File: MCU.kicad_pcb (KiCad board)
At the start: 2 copper layers, 55.9 x 30.5 mm, 55 parts, among them CON1 BARREL_JACK, P1 CONN_01X14, P2 CONN_01X14, P3 CONN_01X09, P4 USB_OTG, P5 CONN_02X05, P6 CONN_01X09, P7 CONN_02X04, P8 USB_OTG, SW1 Reset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

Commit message: Added Analog-Digital Conversion Capability
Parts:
- added C22: 0.1uF, Capacitors_SMD:C_0603, F.Cu at (-8.00, -23.0)
- added C23: 0.1uF, Capacitors_SMD:C_0603, F.Cu at (-12.4, -23.2)
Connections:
- net /LED-Feedback renamed /LED-FB
- U1 pad 13: Net-(U1-Pad13) -> +3V3
- U1 pad 14: Net-(U1-Pad14) -> +3V3
- U1 pad 15: Net-(U1-Pad15) -> GND
- U1 pad 16: Net-(U1-Pad16) -> GND
- U1 pad 17: Net-(U1-Pad17) -> +3V3
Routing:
- net +3V3: track 73.9 -> 83.6 mm
- net GND: track 41.0 -> 41.8 mm, vias 48 -> 51
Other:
- board text removed: "Flash Header"

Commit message: Made PCB more Manufacturer-friendly
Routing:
- net /D-: track 15.1 -> 19.4 mm
- net /PTB19: track 10.2 -> 7.57 mm
- net /PTB18: track 14.2 -> 11.9 mm
- net /PTB17: track 12.9 -> 10.8 mm
- net /PTB16: track 14.2 -> 13.5 mm
- net /INTB: track 5.74 -> 5.02 mm

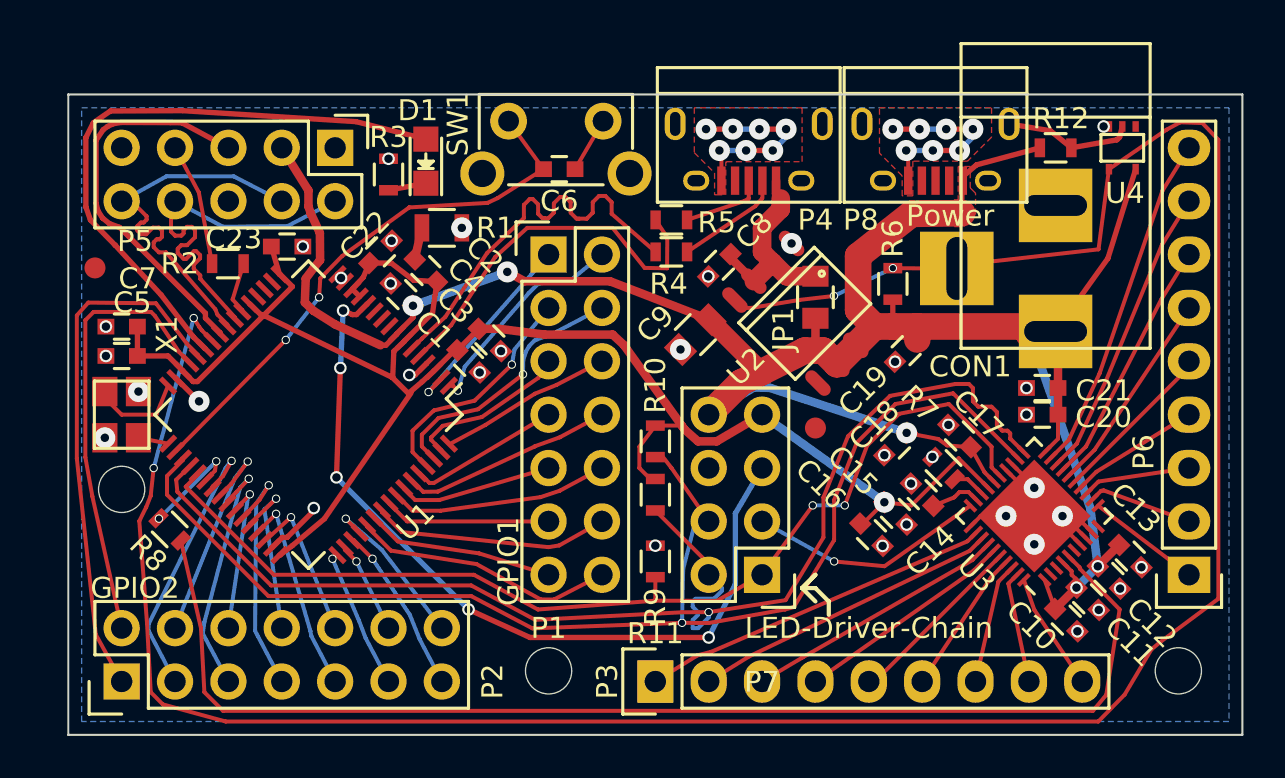
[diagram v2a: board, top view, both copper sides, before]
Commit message: Switched to 2.5mm Mounting Holes
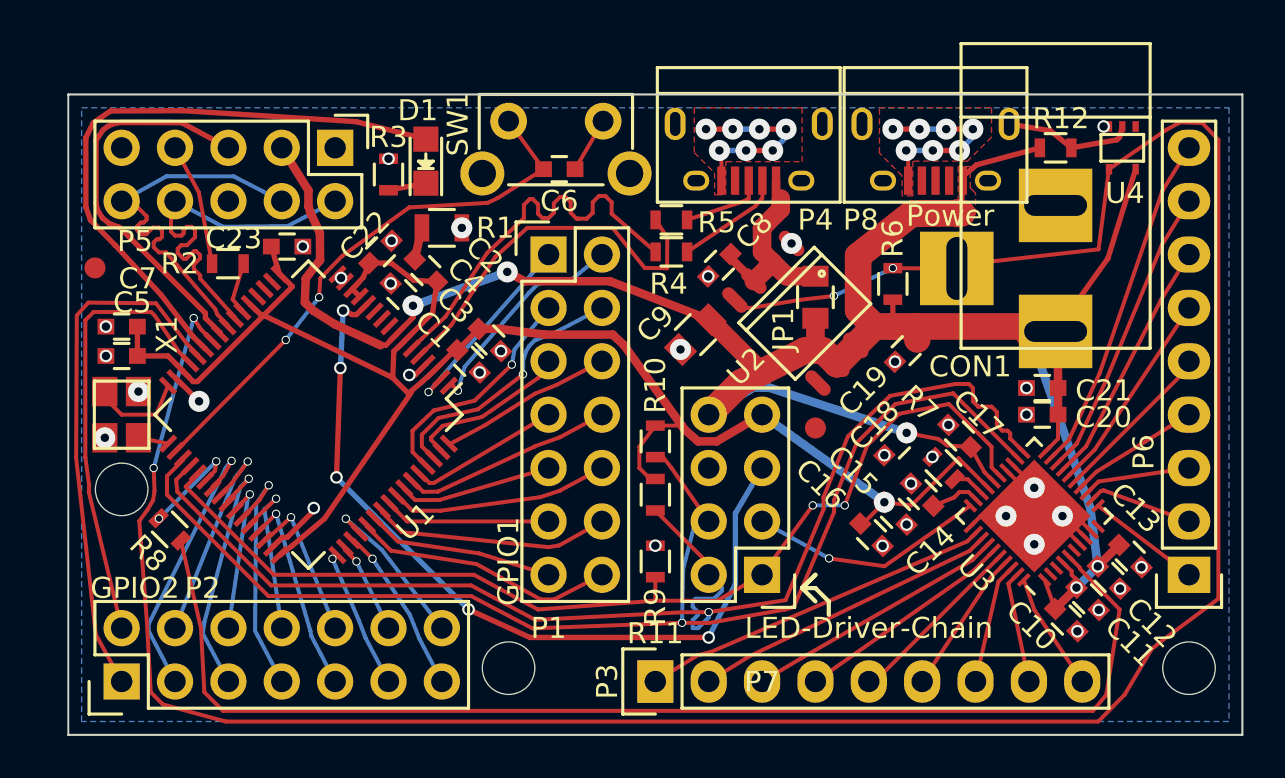
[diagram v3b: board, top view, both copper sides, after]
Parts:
- removed the ? at (-20.3, -11.7)
- removed the ? at (0.00, -3.05)
- removed the ? at (30.0, -3.05)
- added ?: MountingHole_2.5mm, Mounting_Holes:MountingHole_2.5mm, F.Cu at (-20.3, -11.7)
- added ?: MountingHole_2.5mm, Mounting_Holes:MountingHole_2.5mm, F.Cu at (30.5, -3.17)
- added ?: MountingHole_2.5mm, Mounting_Holes:MountingHole_2.5mm, F.Cu at (-1.91, -3.17)

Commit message: More appropriate Placement of Mounting-Holes
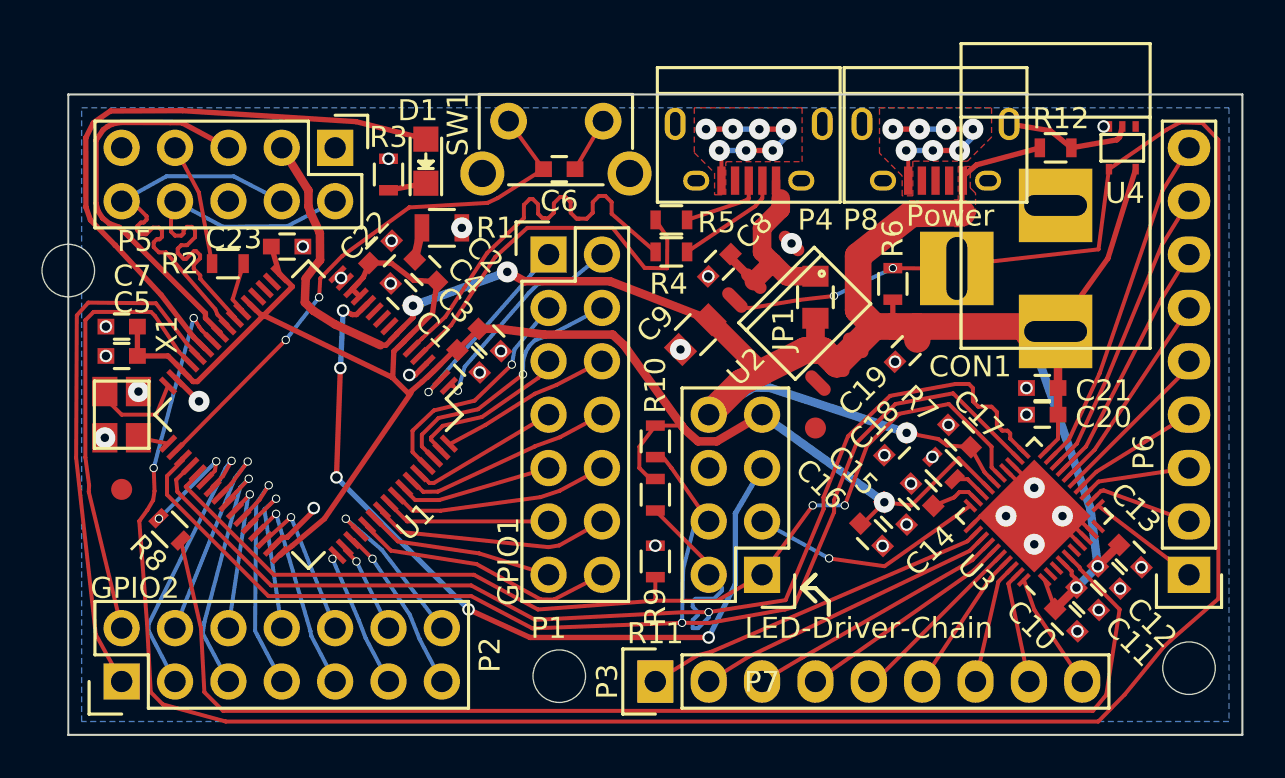
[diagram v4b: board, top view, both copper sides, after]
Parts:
- moved ? 10.7 mm to (-22.9, -22.1)
- moved ? 10.6 mm to (-20.3, -11.7)
- moved ? 2.44 mm to (0.51, -2.79)
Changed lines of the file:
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@@
     (links 185)
     (no_connects 0)
-    (area -38.606296 -33.8682 43.607343 2.571533)
+    (area -22.909551 -30.529551 33.069551 0.049551)
     (thickness 1.6002)
     (drawings 14)
@@
   )
   (module Mounting_Holes:MountingHole_2.5mm (layer Front)
-    (at -20.32 -11.684)
+    (at -22.86 -22.098)
     (descr "Mounting Hole 2.5mm, no annular")
     (tags "mounting hole 2.5mm no annular")
@@
     (descr "Through hole pin header")
     (tags "pin header")
-    (fp_text reference P2 (at 4.445 3.8481 180) (layer F.SilkS)
+    (fp_text reference P2 (at 1.27 17.526 90) (layer F.SilkS)
       (effects (font (size 1 1) (thickness 0.15)))
     )
@@
     (tags "capacitor 0603")
     (attr smd)
-    (fp_text reference C7 (at -0.762 2.286 180) (layer F.SilkS)
+    (fp_text reference C7 (at -0.508 2.413 180) (layer F.SilkS)
       (effects (font (size 1 1) (thickness 0.15)))
     )
@@
   )
   (module Fiducials:Fiducial_1mm_Dia_2.54mm_Outer_CopperTop (layer Front)
-    (at -21.59 -22.225)
+    (at -20.32 -11.684)
     (descr "Circular Fiducial, 1mm bare copper top; 2.54mm keepout")
     (tags marker)
@@
   )
   (module Mounting_Holes:MountingHole_2.5mm (layer Front)
-    (at -1.905 -3.175)
+    (at 0.508 -2.794)
     (descr "Mounting Hole 2.5mm, no annular")
     (tags "mounting hole 2.5mm no annular")
@@
   (segment (start 8.65833 -22.701645) (end 9.767331 -21.592644) (width 0.4064) (layer Front) (net 75) (status 30))
   (segment (start 10.9855 -22.170525) (end 10.665356 -22.490669) (width 0.4064) (layer Front) (net 75) (status 30))
-  (segment (start 27.417892 -1.918801) (end 28.692825 -4.069439) (width 0.19) (layer Front) (net 76))
-  (segment (start 29.107569 -4.41556) (end 31.877 -6.477) (width 0.19) (layer Front) (net 76))
-  (segment (start 28.692825 -4.069439) (end 29.107569 -4.41556) (width 0.19) (layer Front) (net 76))
+  (segment (start 27.417892 -1.918801) (end 29.294566 -4.207434) (width 0.19) (layer Front) (net 76))
+  (segment (start 29.594871 -4.487622) (end 31.877 -6.477) (width 0.19) (layer Front) (net 76))
+  (segment (start 29.294566 -4.207434) (end 29.594871 -4.487622) (width 0.19) (layer Front) (net 76))
   (via (at 13.581769 -20.890666) (size 0.4) (drill 0.3) (layers Front Back) (net 76))
   (segment (start 13.581769 -20.890666) (end 11.938 -20.701) (width 0.19) (layer Front) (net 76))
@@
   (segment (start -18.923 -20.1295) (end -21.6535 -20.1295) (width 0.19) (layer Front) (net 83))
   (segment (start -21.6535 -20.1295) (end -22.0472 -19.7358) (width 0.19) (layer Front) (net 83))
-  (segment (start -20.32 -5.08) (end -20.32 -5.08) (width 0.19) (layer Front) (net 83) (status C00010))
-  (segment (start -20.32 -5.08) (end -21.88622 -11.571404) (width 0.19) (layer Front) (net 83) (status 400010))
+  (segment (start -20.32 -5.08) (end -20.32 -5.08) (width 0.19) (layer Front) (net 83) (status 10))
+  (segment (start -20.32 -5.08) (end -21.88622 -11.571404) (width 0.19) (layer Front) (net 83) (status 10))
   (segment (start -21.88622 -11.571404) (end -21.86785 -11.87411) (width 0.19) (layer Front) (net 83))
   (segment (start -21.86785 -11.87411) (end -22.0472 -13.208) (width 0.19) (layer Front) (net 83))
